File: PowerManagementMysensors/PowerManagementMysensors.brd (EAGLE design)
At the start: 49.5 x 44.1 mm, 52 parts, among them IC2 AT25DF512C-SSHN-B, U1 LM8364BALMF20, U2 SI2399DS-T1-GE3, U3 SI2399DS-T1-GE3, U4 MCP1640BT-I/CHY, U5 TPS61222DCKT

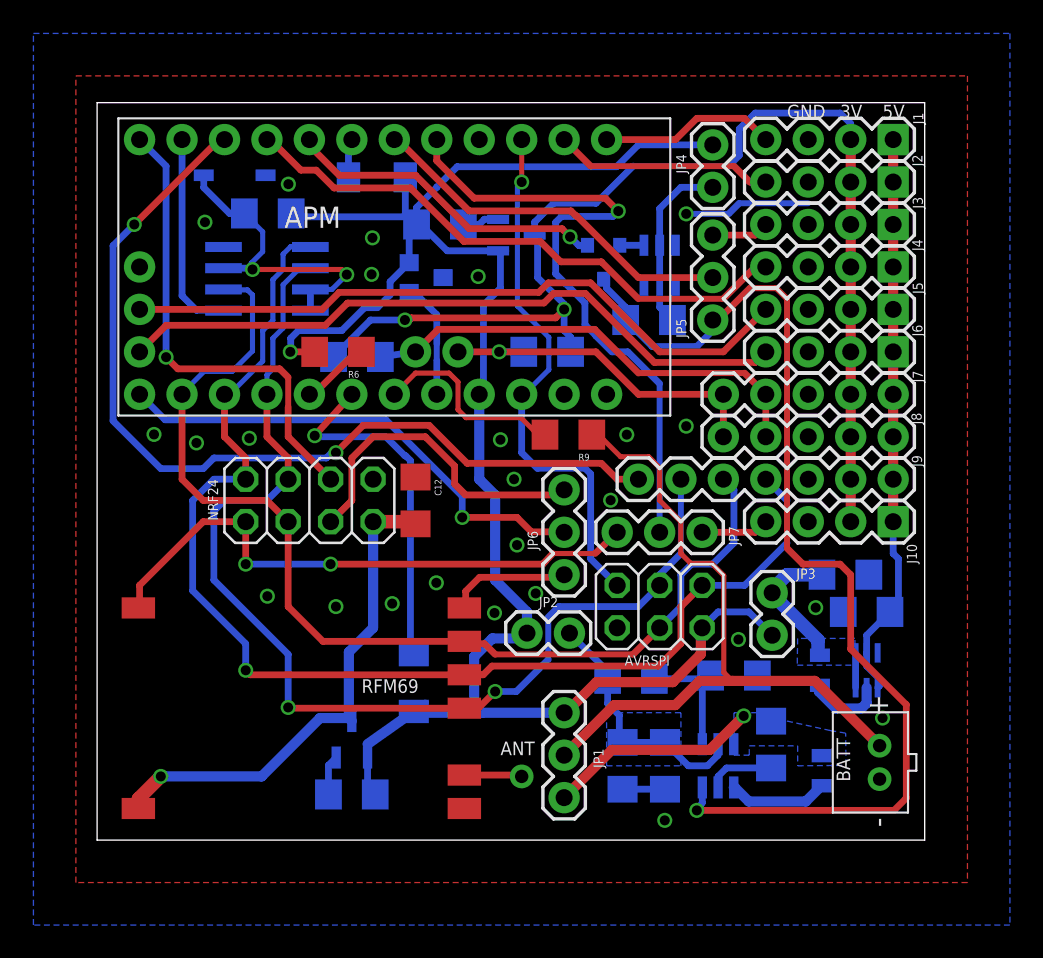
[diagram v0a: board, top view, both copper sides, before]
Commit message: gnd plane under nrf removed
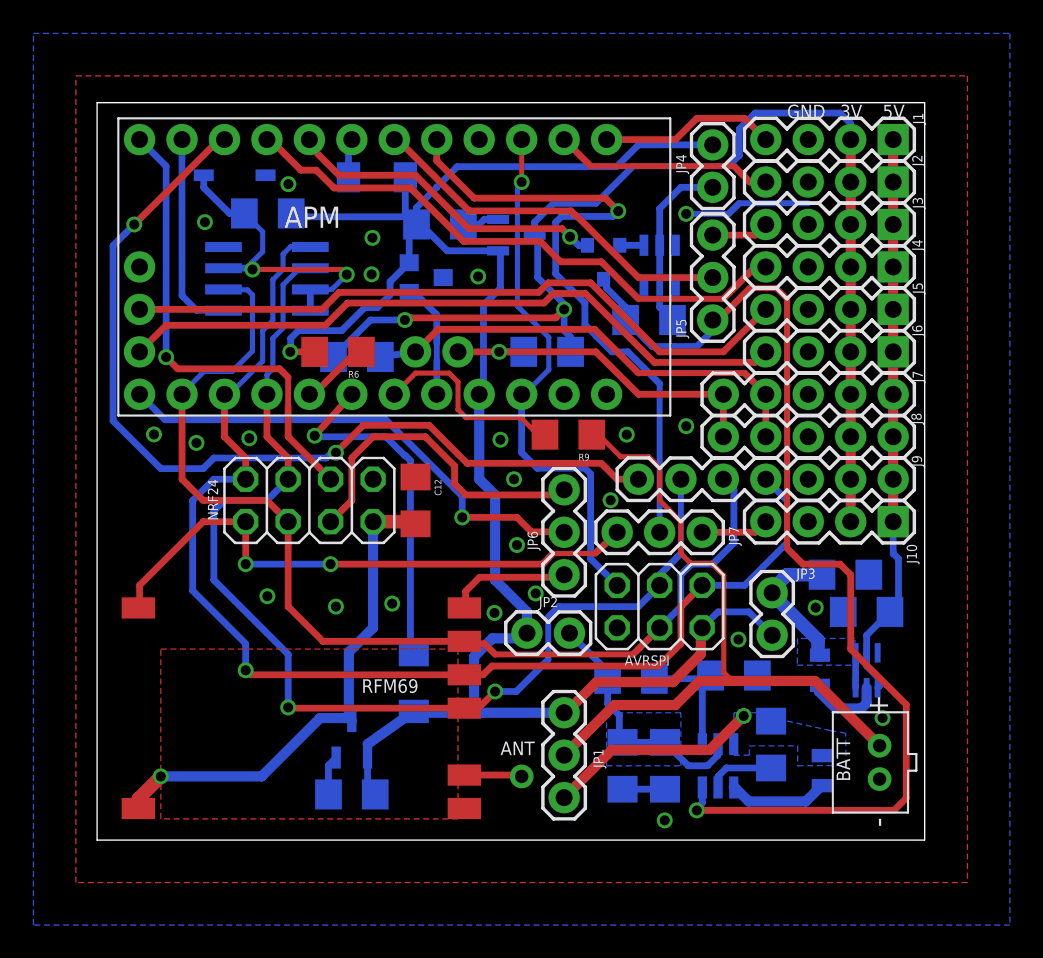
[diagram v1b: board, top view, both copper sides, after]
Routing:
- net GND: vias 25 -> 24
- added copper zone on layer 1, net N$15
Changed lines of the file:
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@@
 </class>
 </classes>
-<designrules name="SeeedStudio_2layer_DRU_no_angle_20140221">
+<designrules name="LaenPCBOrder">
 <description language="de">&lt;b&gt;EAGLE Design Rules&lt;/b&gt;
 &lt;p&gt;
@@
 Einstellungen hier und speichern die Design Rules unter
 einem neuen Namen ab.</description>
-<description language="en">&lt;b&gt;EAGLE Design Rules&lt;/b&gt;
+<description language="en">&lt;b&gt;Laen's PCB Order Design Rules&lt;/b&gt;
 &lt;p&gt;
-The default Design Rules have been set to cover
-a wide range of applications. Your particular design
-may have different requirements, so please make the
-necessary adjustments and save your customized
-design rules under a new name.</description>
-<description language="zh">&lt;b&gt;Seeed Studio EAGLE Design Rules&lt;/b&gt;
-</description>
+Please make sure your boards conform to these design rules.</description>
 <param name="layerSetup" value="(1*16)"/>
-<param name="mtCopper" value="0.035mm 0.0175mm 0.035mm 0.035mm 0.035mm 0.035mm 0.035mm 0.035mm 0.035mm 0.035mm 0.035mm 0.035mm 0.035mm 0.035mm 0.0175mm 0.035mm"/>
-<param name="mtIsolate" value="1.5mm 1.1mm 0.2mm 0.15mm 0.2mm 0.15mm 0.2mm 0.15mm 0.2mm 0.15mm 0.2mm 0.15mm 0.2mm 0.15mm 0.2mm"/>
+<param name="mtCopper" value="0.0356mm 0.0356mm 0.0356mm 0.0356mm 0.0356mm 0.0356mm 0.0356mm 0.0356mm 0.0356mm 0.0356mm 0.0356mm 0.0356mm 0.0356mm 0.0356mm 0.0356mm 0.0356mm"/>
+<param name="mtIsolate" value="1.5011mm 0.1499mm 0.2007mm 0.1499mm 0.2007mm 0.1499mm 0.2007mm 0.1499mm 0.2007mm 0.1499mm 0.2007mm 0.1499mm 0.2007mm 0.1499mm 0.2007mm"/>
 <param name="mdWireWire" value="6mil"/>
 <param name="mdWirePad" value="6mil"/>
@@
 <param name="mdPadVia" value="6mil"/>
 <param name="mdViaVia" value="6mil"/>
-<param name="mdSmdPad" value="0mil"/>
-<param name="mdSmdVia" value="0mil"/>
-<param name="mdSmdSmd" value="0mil"/>
+<param name="mdSmdPad" value="6mil"/>
+<param name="mdSmdVia" value="6mil"/>
+<param name="mdSmdSmd" value="6mil"/>
 <param name="mdViaViaSameLayer" value="8mil"/>
 <param name="mnLayersViaInSmd" value="2"/>
-<param name="mdCopperDimension" value="10mil"/>
-<param name="mdDrill" value="10mil"/>
+<param name="mdCopperDimension" value="15mil"/>
+<param name="mdDrill" value="6mil"/>
 <param name="mdSmdStop" value="0mil"/>
 <param name="msWidth" value="6mil"/>
-<param name="msDrill" value="12mil"/>
-<param name="msMicroVia" value="12mil"/>
+<param name="msDrill" value="13mil"/>
+<param name="msMicroVia" value="13mil"/>
 <param name="msBlindViaRatio" value="0.5"/>
 <param name="rvPadTop" value="0.25"/>
@@
 <param name="rvMicroViaOuter" value="0.25"/>
 <param name="rvMicroViaInner" value="0.25"/>
-<param name="rlMinPadTop" value="10mil"/>
+<param name="rlMinPadTop" value="7mil"/>
 <param name="rlMaxPadTop" value="20mil"/>
-<param name="rlMinPadInner" value="10mil"/>
+<param name="rlMinPadInner" value="7mil"/>
 <param name="rlMaxPadInner" value="20mil"/>
-<param name="rlMinPadBottom" value="10mil"/>
+<param name="rlMinPadBottom" value="7mil"/>
 <param name="rlMaxPadBottom" value="20mil"/>
-<param name="rlMinViaOuter" value="6mil"/>
+<param name="rlMinViaOuter" value="7mil"/>
 <param name="rlMaxViaOuter" value="20mil"/>
-<param name="rlMinViaInner" value="6mil"/>
+<param name="rlMinViaInner" value="7mil"/>
 <param name="rlMaxViaInner" value="20mil"/>
 <param name="rlMinMicroViaOuter" value="4mil"/>
@@
 <param name="psTop" value="-1"/>
 <param name="psBottom" value="-1"/>
-<param name="psFirst" value="0"/>
+<param name="psFirst" value="-1"/>
 <param name="psElongationLong" value="100"/>
 <param name="psElongationOffset" value="100"/>
 <param name="mvStopFrame" value="1"/>
 <param name="mvCreamFrame" value="0"/>
-<param name="mlMinStopFrame" value="2mil"/>
-<param name="mlMaxStopFrame" value="2mil"/>
+<param name="mlMinStopFrame" value="3mil"/>
+<param name="mlMaxStopFrame" value="3mil"/>
 <param name="mlMinCreamFrame" value="0mil"/>
 <param name="mlMaxCreamFrame" value="0mil"/>
-<param name="mlViaStopLimit" value="100mil"/>
+<param name="mlViaStopLimit" value="0mil"/>
 <param name="srRoundness" value="0"/>
 <param name="srMinRoundness" value="0mil"/>
@@
 <param name="checkAngle" value="0"/>
 <param name="checkFont" value="1"/>
-<param name="checkRestrict" value="0"/>
+<param name="checkRestrict" value="1"/>
 <param name="useDiameter" value="13"/>
 <param name="maxErrors" value="50"/>
@@
 <via x="6.4516" y="36.9697" extent="1-16" drill="0.6"/>
 <via x="10.1854" y="14.5923" extent="1-16" drill="0.6"/>
-<via x="20.2946" y="15.3924" extent="1-16" drill="0.6"/>
 <via x="14.2875" y="13.97" extent="1-16" drill="0.6"/>
 <via x="38.3667" y="12.0015" extent="1-16" drill="0.6"/>
@@
 <wire x1="9.906" y1="36.3952" x2="8.8108" y2="37.4904" width="0.3048" layer="16"/>
 </signal>
+<signal name="N$15">
+<polygon width="0" layer="1" pour="cutout">
+<vertex x="3.81" y="11.43"/>
+<vertex x="21.59" y="11.43"/>
+<vertex x="21.59" y="1.27"/>
+<vertex x="3.81" y="1.27"/>
+</polygon>
+</signal>
 </signals>

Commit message: gnd plane modified for nrf24
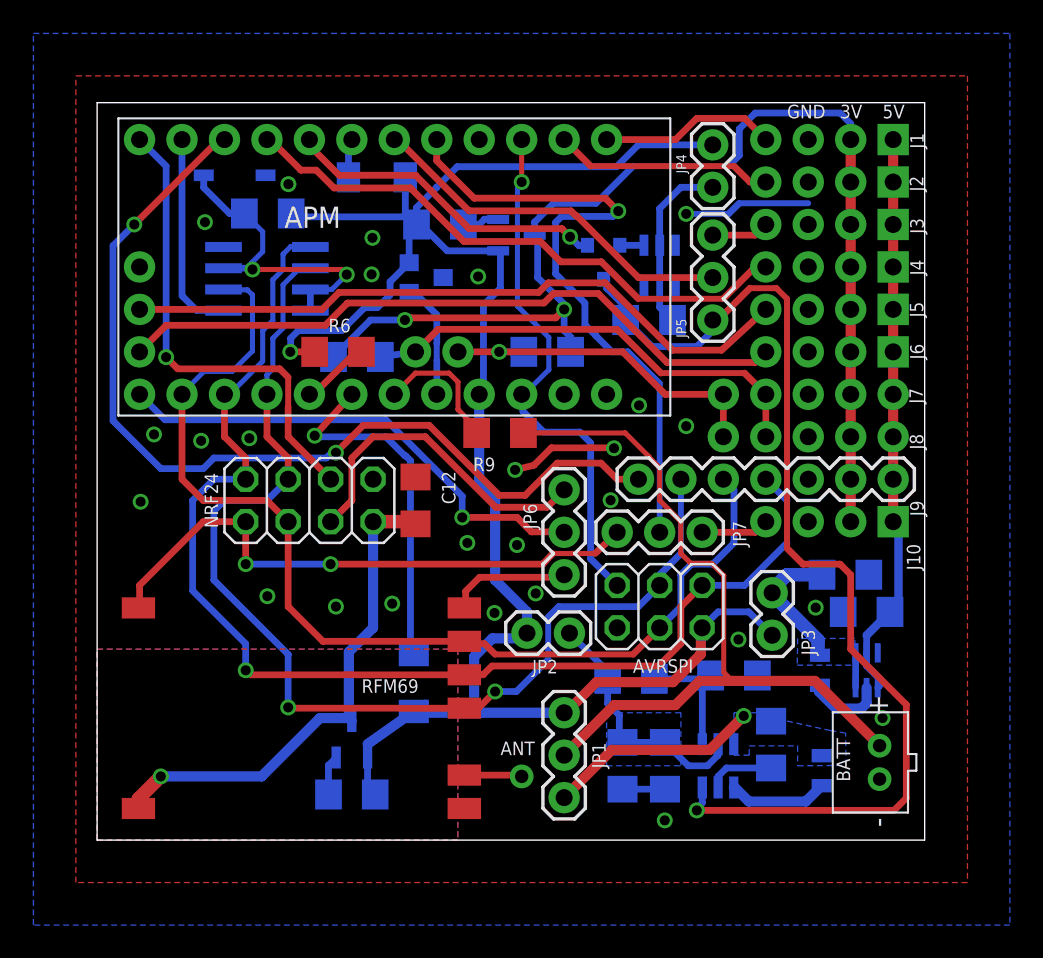
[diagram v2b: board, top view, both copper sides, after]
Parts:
- J1, J10, J2, J3, J4, J5, J6: device SparkFun-Connectors:1X04 -> SparkFun-Connectors:1X04_NO_SILK
- J7, J8: device SparkFun-Connectors:1X05 -> SparkFun-Connectors:1X05_NO_SILK
- moved R9 4.09 mm to (24.1, 24.4)
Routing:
- net GND: track 14.2 -> 20.5 mm, vias 24 -> 26
- net VIN: track 43.1 -> 47.3 mm
- net N$14: track 12.0 -> 8.03 mm
- net SPI_CSN: track 54.8 -> 56.4 mm
- added copper zone on layer 16, net N$16

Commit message: Mosfet + Pull up on LM8364 reset
Pull up on lm8364 was missing. oops. So mosfet and pull up added to
invert signal. Schem changed. Little change for radios gnd plane. BOM
changed
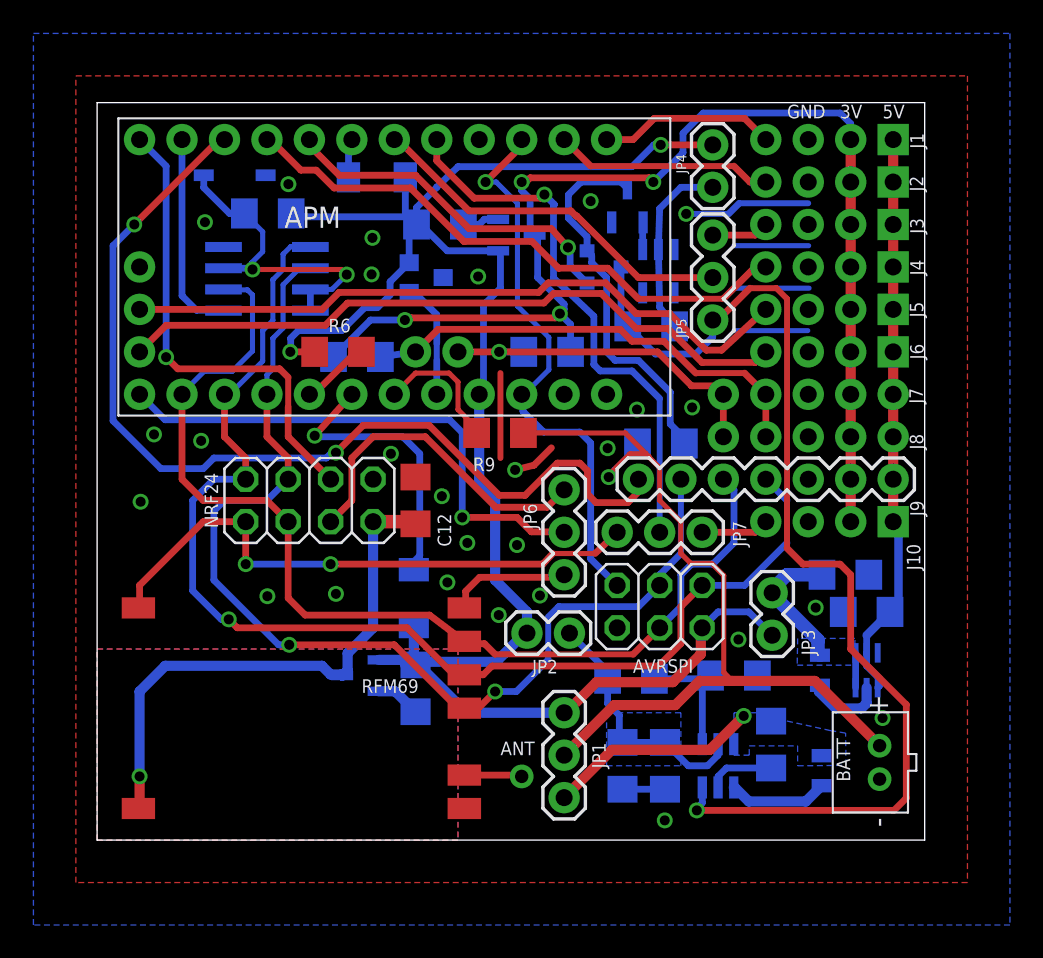
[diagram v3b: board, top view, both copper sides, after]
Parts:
- added R11: 10k, SparkFun-Passives:1206
- added U6: BSS123-7-F, pmo_lib:SOT95P240X110-3N
- moved R5 7.41 mm to (19.1, 9.08), turned to 270 degrees
- moved D2 5.08 mm to (18.9, 14.5)
- moved U3 3.84 mm to (15.7, 9.84), turned to 0 degrees
- moved R4 0.40 mm to (33.1, 30.7)
- moved U1 0.27 mm to (33.6, 34.0)
- moved D6 0.25 mm to (30.3, 34.3), turned to 270 degrees
- renumbered U$5 to ANT
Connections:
- new net N$17: D6.2, R11.1, U6.3
- net GND: now also U6.2
- net N$5: now also U6.1; no longer D6.2
- net VIN: now also R11.2
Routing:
- net N$17: track 0.00 -> 22.6 mm
- net GND: track 20.5 -> 35.3 mm, vias 26 -> 27
- net D2: track 39.1 -> 33.0 mm
- net VIN: track 47.3 -> 53.1 mm, vias 0 -> 1
- net EN_POWERRF: track 21.3 -> 17.1 mm
- net SPI_CSN: track 56.4 -> 58.9 mm
- net VCC_SENSORS: track 70.4 -> 72.8 mm, vias 2 -> 4
- net VCC_RF: track 30.4 -> 32.6 mm
- net D10: track 29.6 -> 31.8 mm
- net RST: track 31.9 -> 33.9 mm
- net SCK: track 67.1 -> 65.3 mm
- net D5_ENBOOST: track 19.5 -> 21.0 mm
- net EN_BOOST: track 63.8 -> 64.9 mm
- net MISO: track 74.0 -> 73.1 mm
- net VCC: track 115.4 -> 114.9 mm, vias 1 -> 2

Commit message: change on mosfet power (error in previous version)
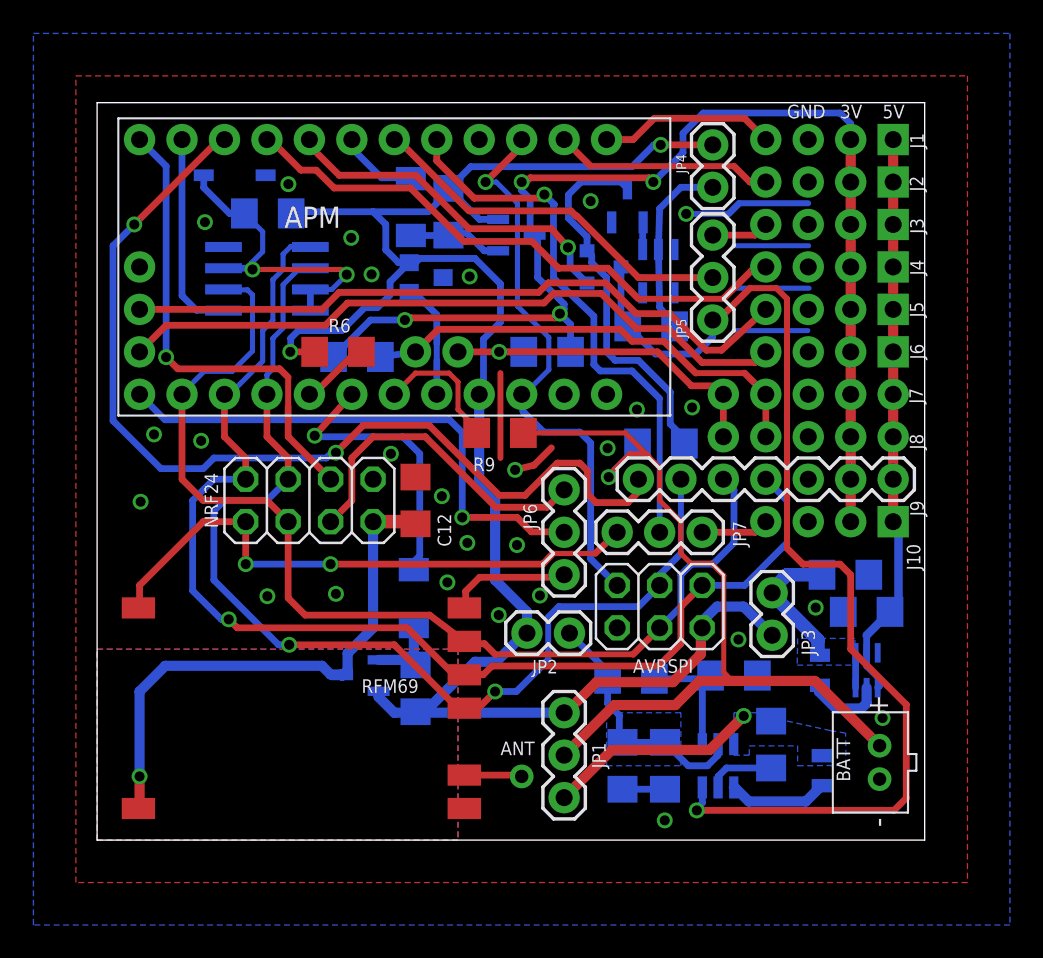
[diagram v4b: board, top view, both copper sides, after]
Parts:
- moved D1 2.70 mm to (18.8, 37.9), turned to 270 degrees
- moved R3 0.92 mm to (21.0, 37.6), turned to 90 degrees
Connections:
- removed net N$3: R3.2, U2.2
- new net N$18: D2.2, R5.1, U3.1
- net N$7: now also D1.2, R3.1, U2.1; no longer R5.2, U3.2
- net VCC: now also R3.2, R5.2, U2.2, U3.2; no longer D1.2, D2.2, R3.1, R5.1, U2.1, U3.1
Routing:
- net N$18: track 0.00 -> 4.67 mm
- net N$7: track 2.72 -> 6.19 mm
- net EN_POWER: track 2.43 -> 4.80 mm
- net N$3: track 2.22 -> 0.00 mm
- net VCC: track 114.9 -> 113.5 mm
